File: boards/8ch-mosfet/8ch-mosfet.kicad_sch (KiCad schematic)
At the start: 7 parts, among them U1 ESP32-DEVKITC, U2 MCP3208

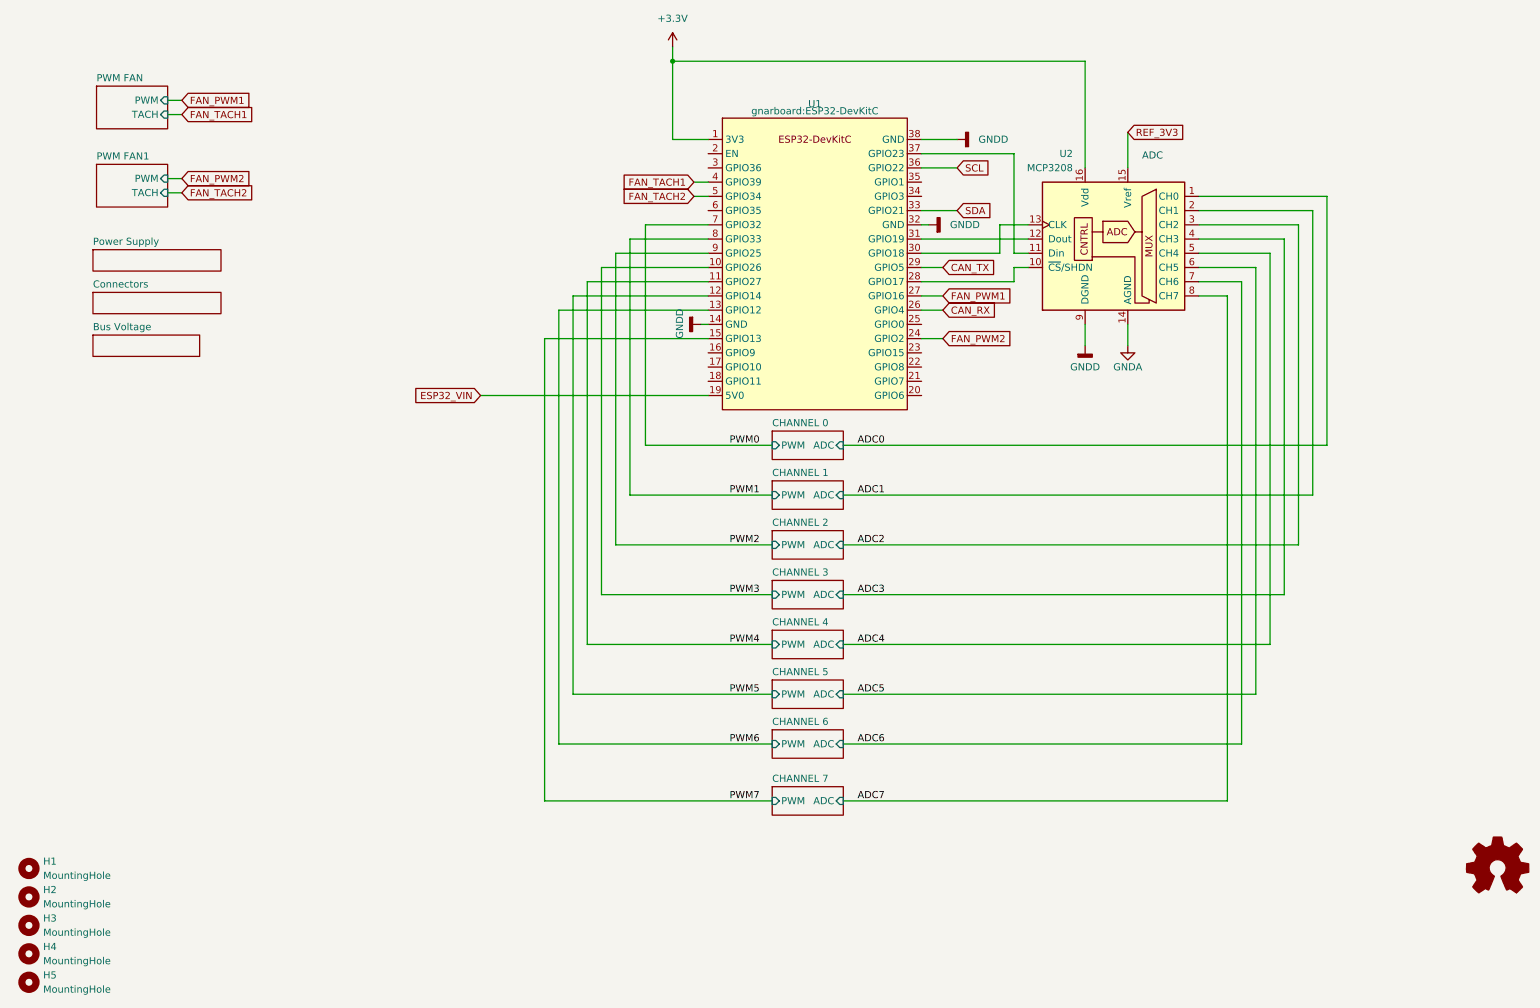
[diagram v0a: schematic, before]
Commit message: updated schematic to pass erc
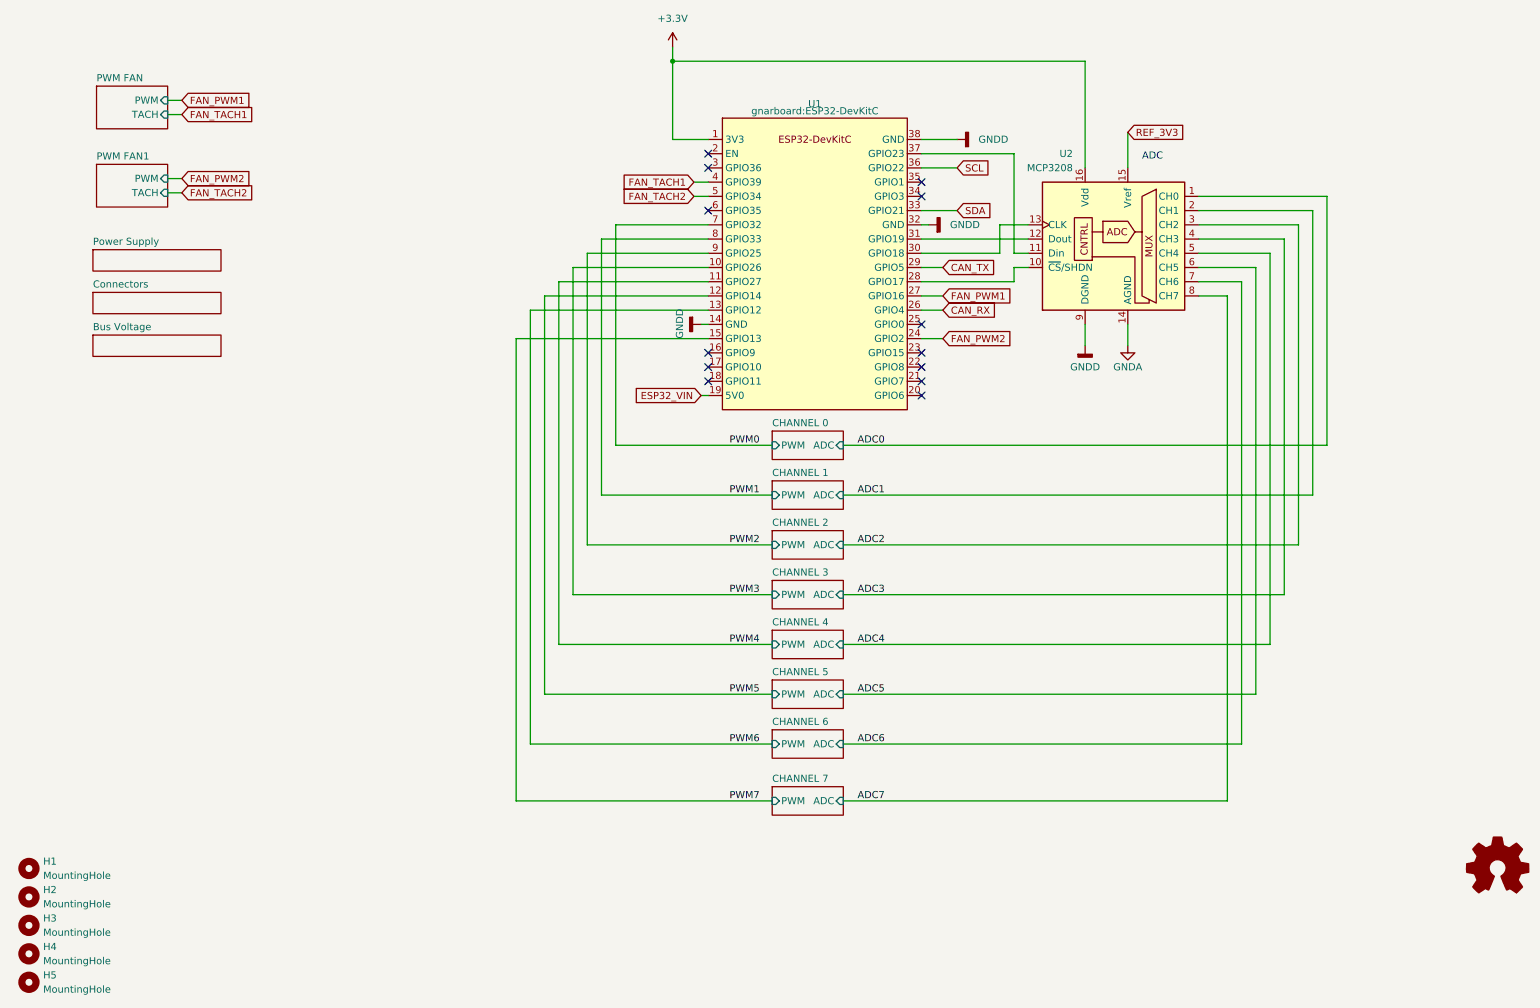
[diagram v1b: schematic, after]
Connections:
- no-connect marks 0 -> 13
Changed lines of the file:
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@@
   (junction (at 130.81 30.48) (diameter 0) (color 0 0 0 0)
   )
+  (no_connect (at 175.26 82.55))
+  (no_connect (at 137.16 46.99))
+  (no_connect (at 175.26 87.63))
+  (no_connect (at 137.16 85.09))
+  (no_connect (at 137.16 87.63))
+  (no_connect (at 137.16 82.55))
+  (no_connect (at 137.16 49.53))
+  (no_connect (at 175.26 54.61))
+  (no_connect (at 175.26 52.07))
+  (no_connect (at 175.26 90.17))
+  (no_connect (at 175.26 77.47))
+  (no_connect (at 137.16 57.15))
+  (no_connect (at 175.26 85.09))
   (wire (pts (xy 134.62 52.07) (xy 137.16 52.07))
     (stroke (width 0) (type default))
@@
     (stroke (width 0) (type default))
   )
-  (wire (pts (xy 115.57 69.85) (xy 137.16 69.85))
+  (wire (pts (xy 110.49 69.85) (xy 137.16 69.85))
     (stroke (width 0) (type default))
   )
@@
     (stroke (width 0) (type default))
   )
-  (wire (pts (xy 113.03 72.39) (xy 113.03 143.51))
+  (wire (pts (xy 107.95 72.39) (xy 107.95 143.51))
     (stroke (width 0) (type default))
   )
@@
     (stroke (width 0) (type default))
   )
-  (wire (pts (xy 107.95 162.56) (xy 148.59 162.56))
+  (wire (pts (xy 102.87 162.56) (xy 148.59 162.56))
     (stroke (width 0) (type default))
   )
@@
     (stroke (width 0) (type default))
   )
-  (wire (pts (xy 115.57 134.62) (xy 148.59 134.62))
-    (stroke (width 0) (type default))
-  )
-  (wire (pts (xy 123.19 62.23) (xy 137.16 62.23))
+  (wire (pts (xy 110.49 134.62) (xy 148.59 134.62))
+    (stroke (width 0) (type default))
+  )
+  (wire (pts (xy 118.11 62.23) (xy 137.16 62.23))
     (stroke (width 0) (type default))
   )
@@
     (stroke (width 0) (type default))
   )
-  (wire (pts (xy 110.49 74.93) (xy 137.16 74.93))
+  (wire (pts (xy 105.41 74.93) (xy 137.16 74.93))
     (stroke (width 0) (type default))
   )
@@
     (stroke (width 0) (type default))
   )
-  (wire (pts (xy 118.11 125.73) (xy 148.59 125.73))
+  (wire (pts (xy 113.03 125.73) (xy 148.59 125.73))
     (stroke (width 0) (type default))
   )
@@
     (stroke (width 0) (type default))
   )
-  (wire (pts (xy 120.65 64.77) (xy 137.16 64.77))
-    (stroke (width 0) (type default))
-  )
-  (wire (pts (xy 125.9584 59.69) (xy 137.16 59.69))
+  (wire (pts (xy 115.57 64.77) (xy 137.16 64.77))
+    (stroke (width 0) (type default))
+  )
+  (wire (pts (xy 120.65 59.69) (xy 137.16 59.69))
     (stroke (width 0) (type default))
   )
@@
     (stroke (width 0) (type default))
   )
-  (wire (pts (xy 107.95 80.01) (xy 137.16 80.01))
+  (wire (pts (xy 102.87 80.01) (xy 137.16 80.01))
     (stroke (width 0) (type default))
   )
@@
     (stroke (width 0) (type default))
   )
-  (wire (pts (xy 120.65 116.84) (xy 148.59 116.84))
-    (stroke (width 0) (type default))
-  )
-  (wire (pts (xy 107.95 80.01) (xy 107.95 162.56))
+  (wire (pts (xy 115.57 116.84) (xy 148.59 116.84))
+    (stroke (width 0) (type default))
+  )
+  (wire (pts (xy 102.87 80.01) (xy 102.87 162.56))
     (stroke (width 0) (type default))
   )
@@
     (stroke (width 0) (type default))
   )
-  (wire (pts (xy 118.11 67.31) (xy 118.11 125.73))
+  (wire (pts (xy 113.03 67.31) (xy 113.03 125.73))
     (stroke (width 0) (type default))
   )
@@
     (stroke (width 0) (type default))
   )
-  (wire (pts (xy 123.19 107.95) (xy 148.59 107.95))
+  (wire (pts (xy 118.11 107.95) (xy 148.59 107.95))
     (stroke (width 0) (type default))
   )
@@
     (stroke (width 0) (type default))
   )
-  (wire (pts (xy 113.03 72.39) (xy 137.16 72.39))
+  (wire (pts (xy 107.95 72.39) (xy 137.16 72.39))
     (stroke (width 0) (type default))
   )
@@
     (stroke (width 0) (type default))
   )
-  (wire (pts (xy 96.52 90.17) (xy 137.16 90.17))
-    (stroke (width 0) (type default))
-  )
-  (wire (pts (xy 123.19 62.23) (xy 123.19 107.95))
-    (stroke (width 0) (type default))
-  )
-  (wire (pts (xy 120.65 64.77) (xy 120.65 116.84))
+  (wire (pts (xy 135.89 90.17) (xy 137.16 90.17))
+    (stroke (width 0) (type default))
+  )
+  (wire (pts (xy 118.11 62.23) (xy 118.11 107.95))
+    (stroke (width 0) (type default))
+  )
+  (wire (pts (xy 115.57 64.77) (xy 115.57 116.84))
     (stroke (width 0) (type default))
   )
@@
     (stroke (width 0) (type default))
   )
-  (wire (pts (xy 115.57 69.85) (xy 115.57 134.62))
+  (wire (pts (xy 110.49 69.85) (xy 110.49 134.62))
     (stroke (width 0) (type default))
   )
@@
     (stroke (width 0) (type default))
   )
-  (wire (pts (xy 125.9584 59.69) (xy 125.9584 99.06))
+  (wire (pts (xy 120.65 59.69) (xy 120.65 99.06))
     (stroke (width 0) (type default))
   )
@@
     (stroke (width 0) (type default))
   )
-  (wire (pts (xy 110.49 152.4) (xy 148.59 152.4))
+  (wire (pts (xy 105.41 152.4) (xy 148.59 152.4))
     (stroke (width 0) (type default))
   )
@@
     (stroke (width 0) (type default))
   )
-  (wire (pts (xy 110.49 74.93) (xy 110.49 152.4))
+  (wire (pts (xy 130.81 30.48) (xy 204.47 30.48))
+    (stroke (width 0) (type default))
+  )
+  (wire (pts (xy 105.41 74.93) (xy 105.41 152.4))
     (stroke (width 0) (type default))
   )
@@
     (stroke (width 0) (type default))
   )
-  (wire (pts (xy 113.03 143.51) (xy 148.59 143.51))
+  (wire (pts (xy 107.95 143.51) (xy 148.59 143.51))
     (stroke (width 0) (type default))
   )
@@
     (stroke (width 0) (type default))
   )
-  (wire (pts (xy 118.11 67.31) (xy 137.16 67.31))
+  (wire (pts (xy 113.03 67.31) (xy 137.16 67.31))
     (stroke (width 0) (type default))
   )
@@
     (stroke (width 0) (type default))
   )
-  (wire (pts (xy 125.9584 99.06) (xy 148.59 99.06))
+  (wire (pts (xy 120.65 99.06) (xy 148.59 99.06))
     (stroke (width 0) (type default))
   )
@@
     (stroke (width 0) (type default))
   )
-  (wire (pts (xy 130.81 30.48) (xy 204.47 30.48))
-    (stroke (width 0) (type default))
-  )
   (text "ADC" (at 214.63 48.26 0)
     (effects (font (size 1.27 1.27)) (justify left bottom))
@@
     )
   )
-  (global_label "ESP32_VIN" (shape input) (at 96.52 90.17 180) (fields_autoplaced)
+  (global_label "ESP32_VIN" (shape input) (at 135.89 90.17 180) (fields_autoplaced)
     (effects (font (size 1.27 1.27)) (justify right))
-    (property "Intersheetrefs" "${INTERSHEET_REFS}" (at 83.4958 90.17 0)
+    (property "Intersheetrefs" "${INTERSHEET_REFS}" (at 122.8658 90.17 0)
       (effects (font (size 1.27 1.27)) (justify right) hide)
     )
@@
     )
   )
-  (sheet (at 27.305 79.375) (size 19.05 3.81) (fields_autoplaced)
-    (stroke (width 0.1524) (type solid))
-    (fill (color 0 0 0 0.0000))
+  (sheet (at 27.305 79.375) (size 22.86 3.81) (fields_autoplaced)
+    (stroke (width 0.1524) (type solid))
+    (fill (color 0 0 0 0.0000))

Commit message: tidied up the schematic
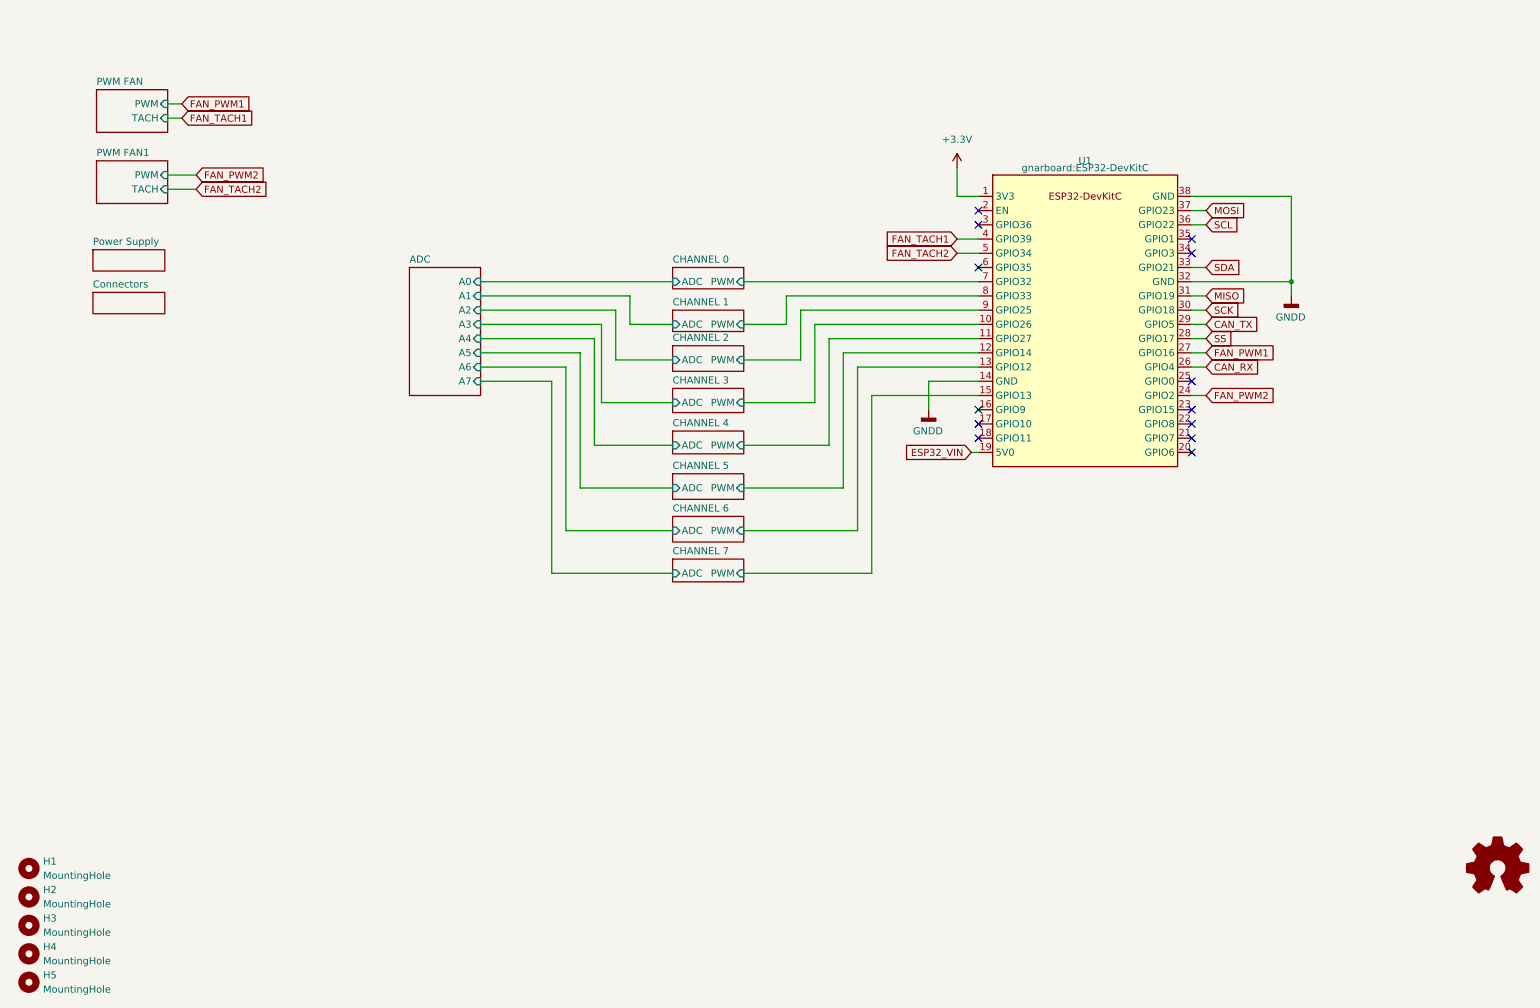
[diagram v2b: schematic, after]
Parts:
- removed U2: MCP3208, Package_SO:SOIC-16_3.9x9.9mm_P1.27mm, symbol Analog_ADC:MCP3208
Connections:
- net SS: now reaches U1.28 (GPIO17)
- net MOSI: now reaches U1.37 (GPIO23)
- net MISO: now reaches U1.31 (GPIO19)
- net SCK: now reaches U1.30 (GPIO18)
- net PWM0 renamed CHANNEL 0/PWM
- net PWM1 renamed CHANNEL 1/PWM
- net PWM2 renamed CHANNEL 2/PWM
- net PWM3 renamed CHANNEL 3/PWM
- net PWM4 renamed CHANNEL 4/PWM
- net PWM5 renamed CHANNEL 5/PWM
- net PWM6 renamed CHANNEL 6/PWM
- net PWM7 renamed CHANNEL 7/PWM
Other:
- sheet Bus Voltage renamed ADC
- sheet ADC: file bus voltage.kicad_sch -> adc.kicad_sch
- sheet ADC ports: added A0, A1, A2, A3, A4, A5, A6, A7; removed none
- note removed: "ADC"
- moved on the sheet: U1

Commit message: tested the bus voltage stuff a bit more
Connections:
- net ESP32_VIN renamed ESP32_5V
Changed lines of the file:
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@@
     )
   )
-  (global_label "ESP32_VIN" (shape input) (at 184.15 100.33 180) (fields_autoplaced)
+  (global_label "ESP32_5V" (shape input) (at 184.15 100.33 180) (fields_autoplaced)
     (effects (font (size 1.27 1.27)) (justify right))
-    (property "Intersheetrefs" "${INTERSHEET_REFS}" (at 171.1258 100.33 0)
+    (property "Intersheetrefs" "${INTERSHEET_REFS}" (at 171.8516 100.33 0)
       (effects (font (size 1.27 1.27)) (justify right) hide)
     )
